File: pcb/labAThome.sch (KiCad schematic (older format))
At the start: 57 parts, among them J1 BME280, J10 SRV2, J11 GND, J2 SRV1, J3 5V, J4 24V IN, J5 SW&LED, J6 R1_CONN, J7 R2_CONN, J8 R3_CONN, J9 FAN, K1 G5V-2, K2 G5V-2, K3 G5V-2, Q1 IRLZ44N, Q2 IRLZ44N, Q3 IRLZ44N, SW1 RED, SW2 GREEN, SW3 BLACK, SW4 BLUE, SW5 WHITE, U1 HC-SR501, U2 24V->5V, U3 24V->3V3, U4 ESP32_DEVKITC_COMPATIBLE, U5 NE555

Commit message: Improved Layout
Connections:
- net labels added: 24V_PERM, Q1_D, Q2_D, R8_D4
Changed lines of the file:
@@
 	11150 6500 7500 6500
-Wire Notes Line
-	7300 6500 7300 2150
 Wire Notes Line
 	7500 2150 11150 2150
@@
 Wire Wire Line
 	7700 3700 7850 3700
+Text Label 7950 750  0    50   ~ 0
+24V_PERM
+Text Label 7550 1050 0    50   ~ 0
+Q2_D
+Text Label 6300 950  0    50   ~ 0
+Q1_D
+Text Label 6800 750  0    50   ~ 0
+R8_D4
+Wire Notes Line
+	7300 6500 7300 2150
 $EndSCHEMATC

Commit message: PCB REV2
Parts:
- removed C1: 100u, Capacitor_THT:CP_Radial_D5.0mm_P2.50mm, symbol Device:CP
- removed C2: 10n, Capacitor_THT:C_Disc_D5.0mm_W2.5mm_P2.50mm, symbol Device:C
- removed C3: u1, Capacitor_THT:C_Disc_D5.0mm_W2.5mm_P5.00mm, symbol Device:C
- removed J11: GND, Connector_PinHeader_2.54mm:PinHeader_1x08_P2.54mm_Vertical, symbol Connector_Generic:Conn_01x08
- removed R2: GL5528, OptoDevice:R_LDR_5.0x4.1mm_P3mm_Vertical, symbol Device:R_PHOTO
- removed U5: NE555, Package_DIP:DIP-8_W7.62mm, symbol Timer:NE555
- added J12: IO, Connector_PinHeader_2.54mm:PinHeader_2x04_P2.54mm_Vertical, symbol Connector_Generic:Conn_02x04_Odd_Even
- added Q4: BC547, Package_TO_SOT_THT:TO-92_Inline, symbol Transistor_BJT:BC547
- added R2: 3k3, Resistor_THT:R_Axial_DIN0207_L6.3mm_D2.5mm_P10.16mm_Horizontal, symbol Device:R
- added U6: GY-302, smopla:GY-302, symbol smopla:GY-302
- R1: value 10K -> 2k2
- R12: value 10k -> 1K
- RV1: value 100k -> R_POT
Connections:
- net labels added: IO0, IO1, IO2, IO3, IO4, IO5, POTI_T, R3_ON
- net labels removed: BRIGHTNESS
- wire segments 68 -> 42
- no-connect marks 23 -> 14
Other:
- note added: "check https://randomnerdtutorials.com/esp32-pinout-reference-gpios/"
- moved on the sheet: J1

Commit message: PCB V2 RC1
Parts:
- removed D5: 1N4001, Diode_THT:D_DO-41_SOD81_P10.16mm_Horizontal, symbol Diode:1N4001
- removed J12: IO, Connector_PinHeader_2.54mm:PinHeader_2x04_P2.54mm_Vertical, symbol Connector_Generic:Conn_02x04_Odd_Even
- removed J4: 24V IN, Connector_BarrelJack:BarrelJack_Horizontal, symbol Connector:Barrel_Jack_Switch
- removed Q1: IRLZ44N, Package_TO_SOT_THT:TO-220-3_Horizontal_TabDown, symbol Device:Q_NMOS_GDS
- removed R7: 10K, Resistor_THT:R_Axial_DIN0207_L6.3mm_D2.5mm_P10.16mm_Horizontal, symbol Device:R
- removed R8: 5R 1W, Resistor_THT:R_Axial_DIN0414_L11.9mm_D4.5mm_P15.24mm_Horizontal, symbol Device:R
- removed U3: 24V->3V3, sensact:MODULE_STEPDOWN, symbol sensact:MODULE_STEPDOWN
- added BZ1: Buzzer, Buzzer_Beeper:Buzzer_12x9.5RM7.6, symbol Device:Buzzer
- added J11: -, smopla:Banana_Jack_2mm, symbol Connector:Conn_01x01_Female
- added J12: FA2, Connector_PinHeader_2.54mm:PinHeader_1x03_P2.54mm_Vertical, symbol Connector_Generic:Conn_01x03
- added J13: Barrel_Jack_Switch, Connector_BarrelJack:BarrelJack_Horizontal, symbol Connector:Barrel_Jack_Switch
- added J14: FA3, Connector_PinHeader_2.54mm:PinHeader_1x03_P2.54mm_Vertical, symbol Connector_Generic:Conn_01x03
- added J4: +, smopla:Banana_Jack_2mm, symbol Connector:Conn_01x01_Female
- added JP2: 5V_ESP, Connector_PinHeader_2.54mm:PinHeader_1x02_P2.54mm_Vertical, symbol Device:Jumper_NO_Small
- added JP3: 3V3_5V, Jumper:SolderJumper-3_P2.0mm_Open_TrianglePad1.0x1.5mm_NumberLabels, symbol Jumper:SolderJumper_3_Open
- added U3: PDC004_Module, smopla:PDC004_Module, symbol smopla:PDC004_Module
- added U5: LD06AJSA, smopla:LD06AJSA, symbol smopla:LD06AJSA
- added U7: IPS_240_240, smopla:IPS_240_240, symbol smopla:IPS_240_240
- added U8: INMP441_Module, smopla:INMP441_Module, symbol smopla:INMP441_Module
- J9: value FAN -> FA1
- JP1: value 5V_LOCAL -> 5V_EXT
- R6: value 1K -> K1
- RV1: value R_POT -> DELAY_TIME
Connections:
- net labels added: BUZZER, FAN_SWITCH, I2S_SCK, I2S_SD, I2S_WS, LCD_BL, LCD_CLK, LCD_DC, LCD_MOSI
- net labels removed: 24V_PERM, IO0, IO1, IO2, IO3, IO4, IO5, Q1_D, R8_D4
- wire segments 42 -> 45
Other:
- note added: "Frei"
- note added: "Input Only"
- note added: "Input Only No Pull"
- note added: "Muss CLK"
- note added: "PULLED UP"
- note added: "Soll LED"
- note added: "Soll SW"
- note added: "WPD Soll Mosfet"
- moved on the sheet: D4, D8, J1, J10, J2, J3, J6, J7, J9, Q2, Q3, Q4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

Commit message: PCB V2 RC2
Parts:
- removed J11: -, smopla:Banana_Jack_2mm, symbol Connector:Conn_01x01_Female
- removed J4: +, smopla:Banana_Jack_2mm, symbol Connector:Conn_01x01_Female
- R1, R10, R12, R13, R14, R15, R16, R2, R3, R4, R5, R6, R9: footprint Resistor_THT:R_Axial_DIN0207_L6.3mm_D2.5mm_P10.16mm_Horizontal -> Resistor_THT:R_Axial_DIN0207_L6.3mm_D2.5mm_P7.62mm_Horizontal
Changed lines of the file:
@@
 F 0 "R3" V 1293 2100 50  0000 C CNN
 F 1 "68R" V 1384 2100 50  0000 C CNN
-F 2 "Resistor_THT:R_Axial_DIN0207_L6.3mm_D2.5mm_P10.16mm_Horizontal" V 1430 2100 50  0001 C CNN
+F 2 "Resistor_THT:R_Axial_DIN0207_L6.3mm_D2.5mm_P7.62mm_Horizontal" V 1430 2100 50  0001 C CNN
 F 3 "~" H 1500 2100 50  0001 C CNN
 	1    1500 2100
@@
 F 0 "R4" V 1293 2450 50  0000 C CNN
 F 1 "68R" V 1384 2450 50  0000 C CNN
-F 2 "Resistor_THT:R_Axial_DIN0207_L6.3mm_D2.5mm_P10.16mm_Horizontal" V 1430 2450 50  0001 C CNN
+F 2 "Resistor_THT:R_Axial_DIN0207_L6.3mm_D2.5mm_P7.62mm_Horizontal" V 1430 2450 50  0001 C CNN
 F 3 "~" H 1500 2450 50  0001 C CNN
 	1    1500 2450
@@
 F 0 "R5" V 1293 2850 50  0000 C CNN
 F 1 "68R" V 1384 2850 50  0000 C CNN
-F 2 "Resistor_THT:R_Axial_DIN0207_L6.3mm_D2.5mm_P10.16mm_Horizontal" V 1430 2850 50  0001 C CNN
+F 2 "Resistor_THT:R_Axial_DIN0207_L6.3mm_D2.5mm_P7.62mm_Horizontal" V 1430 2850 50  0001 C CNN
 F 3 "~" H 1500 2850 50  0001 C CNN
 	1    1500 2850
@@
 F 0 "R14" V 9143 6350 50  0000 C CNN
 F 1 "K1" V 9234 6350 50  0000 C CNN
-F 2 "Resistor_THT:R_Axial_DIN0207_L6.3mm_D2.5mm_P10.16mm_Horizontal" V 9280 6350 50  0001 C CNN
+F 2 "Resistor_THT:R_Axial_DIN0207_L6.3mm_D2.5mm_P7.62mm_Horizontal" V 9280 6350 50  0001 C CNN
 F 3 "~" H 9350 6350 50  0001 C CNN
 	1    9350 6350
@@
 F 0 "R13" V 9143 5950 50  0000 C CNN
 F 1 "K1" V 9234 5950 50  0000 C CNN
-F 2 "Resistor_THT:R_Axial_DIN0207_L6.3mm_D2.5mm_P10.16mm_Horizontal" V 9280 5950 50  0001 C CNN
+F 2 "Resistor_THT:R_Axial_DIN0207_L6.3mm_D2.5mm_P7.62mm_Horizontal" V 9280 5950 50  0001 C CNN
 F 3 "~" H 9350 5950 50  0001 C CNN
 	1    9350 5950
@@
 F 0 "R10" V 7200 1400 50  0000 C CNN
 F 1 "10K" V 7300 1400 50  0000 C CNN
-F 2 "Resistor_THT:R_Axial_DIN0207_L6.3mm_D2.5mm_P10.16mm_Horizontal" V 7230 1400 50  0001 C CNN
+F 2 "Resistor_THT:R_Axial_DIN0207_L6.3mm_D2.5mm_P7.62mm_Horizontal" V 7230 1400 50  0001 C CNN
 F 3 "~" H 7300 1400 50  0001 C CNN
 	1    7300 1400
@@
 F 0 "R9" V 7000 1250 50  0000 C CNN
 F 1 "1K" V 7100 1250 50  0000 C CNN
-F 2 "Resistor_THT:R_Axial_DIN0207_L6.3mm_D2.5mm_P10.16mm_Horizontal" V 7030 1250 50  0001 C CNN
+F 2 "Resistor_THT:R_Axial_DIN0207_L6.3mm_D2.5mm_P7.62mm_Horizontal" V 7030 1250 50  0001 C CNN
 F 3 "~" H 7100 1250 50  0001 C CNN
 	1    7100 1250
@@
 F 0 "R16" V 8550 1400 50  0000 C CNN
 F 1 "10K" V 8650 1400 50  0000 C CNN
-F 2 "Resistor_THT:R_Axial_DIN0207_L6.3mm_D2.5mm_P10.16mm_Horizontal" V 8580 1400 50  0001 C CNN
+F 2 "Resistor_THT:R_Axial_DIN0207_L6.3mm_D2.5mm_P7.62mm_Horizontal" V 8580 1400 50  0001 C CNN
 F 3 "~" H 8650 1400 50  0001 C CNN
 	1    8650 1400
@@
 F 0 "R15" V 8350 1250 50  0000 C CNN
 F 1 "1K" V 8450 1250 50  0000 C CNN
-F 2 "Resistor_THT:R_Axial_DIN0207_L6.3mm_D2.5mm_P10.16mm_Horizontal" V 8380 1250 50  0001 C CNN
+F 2 "Resistor_THT:R_Axial_DIN0207_L6.3mm_D2.5mm_P7.62mm_Horizontal" V 8380 1250 50  0001 C CNN
 F 3 "~" H 8450 1250 50  0001 C CNN
 	1    8450 1250
@@
 F 0 "R12" V 8400 4050 50  0000 C CNN
 F 1 "1K" V 8500 4050 50  0000 C CNN
-F 2 "Resistor_THT:R_Axial_DIN0207_L6.3mm_D2.5mm_P10.16mm_Horizontal" V 8430 4050 50  0001 C CNN
+F 2 "Resistor_THT:R_Axial_DIN0207_L6.3mm_D2.5mm_P7.62mm_Horizontal" V 8430 4050 50  0001 C CNN
 F 3 "~" H 8500 4050 50  0001 C CNN
 	1    8500 4050
@@
 F 0 "R1" V 10200 5050 50  0000 C CNN
 F 1 "2k2" V 10300 5050 50  0000 C CNN
-F 2 "Resistor_THT:R_Axial_DIN0207_L6.3mm_D2.5mm_P10.16mm_Horizontal" V 10230 5050 50  0001 C CNN
+F 2 "Resistor_THT:R_Axial_DIN0207_L6.3mm_D2.5mm_P7.62mm_Horizontal" V 10230 5050 50  0001 C CNN
 F 3 "~" H 10300 5050 50  0001 C CNN
 	1    10300 5050
@@
 F 0 "R2" V 10200 5350 50  0000 C CNN
 F 1 "3k3" V 10300 5350 50  0000 C CNN
-F 2 "Resistor_THT:R_Axial_DIN0207_L6.3mm_D2.5mm_P10.16mm_Horizontal" V 10230 5350 50  0001 C CNN
+F 2 "Resistor_THT:R_Axial_DIN0207_L6.3mm_D2.5mm_P7.62mm_Horizontal" V 10230 5350 50  0001 C CNN
 F 3 "~" H 10300 5350 50  0001 C CNN
 	1    10300 5350
@@
 F 0 "R6" V 1100 5400 50  0000 C CNN
 F 1 "K1" V 1200 5400 50  0000 C CNN
-F 2 "Resistor_THT:R_Axial_DIN0207_L6.3mm_D2.5mm_P10.16mm_Horizontal" V 1130 5400 50  0001 C CNN
+F 2 "Resistor_THT:R_Axial_DIN0207_L6.3mm_D2.5mm_P7.62mm_Horizontal" V 1130 5400 50  0001 C CNN
 F 3 "~" H 1200 5400 50  0001 C CNN
 	1    1200 5400
@@
 Wire Wire Line
 	1400 3250 1800 3250
-$Comp
-L Connector:Conn_01x01_Female J4
-U 1 1 5EE6991E
-P 3500 1500
-F 0 "J4" H 3528 1526 50  0000 L CNN
-F 1 "+" H 3700 1500 50  0000 L CNN
-F 2 "smopla:Banana_Jack_2mm" H 3500 1500 50  0001 C CNN
-F 3 "~" H 3500 1500 50  0001 C CNN
-	1    3500 1500
-	1    0    0    -1
-$EndComp
-$Comp
-L Connector:Conn_01x01_Female J11
-U 1 1 5EE6A720
-P 3500 1600
-F 0 "J11" H 3528 1626 50  0000 L CNN
-F 1 "-" H 3700 1600 50  0000 L CNN
-F 2 "smopla:Banana_Jack_2mm" H 3500 1600 50  0001 C CNN
-F 3 "~" H 3500 1600 50  0001 C CNN
-	1    3500 1600
-	1    0    0    -1
-$EndComp
 Wire Wire Line
 	3050 1500 3300 1500
-Connection ~ 3300 1500
 Wire Wire Line
 	3300 1600 3050 1600
-Connection ~ 3300 1600
 $Comp
 L Connector_Generic:Conn_01x03 J12

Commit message: PCB V2 as ordered
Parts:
- added J4: EXTENSION, Connector_JST:JST_XH_B4B-XH-A_1x04_P2.50mm_Vertical, symbol Connector:Conn_01x04_Male
- added SW6: FAN, smopla:MTS-102, symbol Switch:SW_SPDT
- U7: value IPS_240_240 -> Display
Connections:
- net +5V: now also J4.1 (Pin_1)
- net GND: now also J4.4 (Pin_4), SW6.2 (B); no longer J12.1 (Pin_1)
- net R3_12: now also J14.2 (Pin_2)
- net R3_22: no longer J14.2 (Pin_2)
- net SCL: now also J4.3 (Pin_3)
- net SDA: now also J4.2 (Pin_2)
- new net: J12.1 (Pin_1), SW6.3 (C)
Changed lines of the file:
@@
 P 1300 7150
 F 0 "U7" H 1528 7001 50  0000 L CNN
-F 1 "IPS_240_240" H 1528 6910 50  0000 L CNN
+F 1 "Display" H 1528 6910 50  0000 L CNN
 F 2 "smopla:IPS_240_240" H 1300 7150 50  0001 C CNN
 F 3 "" H 1300 7150 50  0001 C CNN
@@
 L power:GND #PWR048
 U 1 1 5EEDC087
-P 10400 1400
-F 0 "#PWR048" H 10400 1150 50  0001 C CNN
-F 1 "GND" V 10405 1272 50  0000 R CNN
-F 2 "" H 10400 1400 50  0001 C CNN
-F 3 "" H 10400 1400 50  0001 C CNN
-	1    10400 1400
+P 10000 1300
+F 0 "#PWR048" H 10000 1050 50  0001 C CNN
+F 1 "GND" V 10005 1172 50  0000 R CNN
+F 2 "" H 10000 1300 50  0001 C CNN
+F 3 "" H 10000 1300 50  0001 C CNN
+	1    10000 1300
 	0    1    1    0
 $EndComp
@@
 NoConn ~ 8150 3750
 Text GLabel 8150 3650 0    50   BiDi ~ 0
-R3_22
+R3_12
+$Comp
+L Switch:SW_SPDT SW6
+U 1 1 5EED61B0
+P 10200 1300
+F 0 "SW6" H 10200 1585 50  0000 C CNN
+F 1 "FAN" H 10200 1494 50  0000 C CNN
+F 2 "smopla:MTS-102" H 10200 1300 50  0001 C CNN
+F 3 "~" H 10200 1300 50  0001 C CNN
+	1    10200 1300
+	1    0    0    -1
+$EndComp
+$Comp
+L Connector:Conn_01x04_Male J4
+U 1 1 5EF6E56D
+P 1800 4800
+F 0 "J4" H 1772 4774 50  0000 R CNN
+F 1 "EXTENSION" H 1772 4683 50  0000 R CNN
+F 2 "Connector_JST:JST_XH_B4B-XH-A_1x04_P2.50mm_Vertical" H 1800 4800 50  0001 C CNN
+F 3 "~" H 1800 4800 50  0001 C CNN
+	1    1800 4800
+	-1   0    0    -1
+$EndComp
+Text GLabel 1600 4800 0    50   BiDi ~ 0
+SDA
+$Comp
+L power:GND #PWR050
+U 1 1 5EF73FB6
+P 1600 5000
+F 0 "#PWR050" H 1600 4750 50  0001 C CNN
+F 1 "GND" V 1605 4872 50  0000 R CNN
+F 2 "" H 1600 5000 50  0001 C CNN
+F 3 "" H 1600 5000 50  0001 C CNN
+	1    1600 5000
+	0    1    1    0
+$EndComp
+Text GLabel 1600 4900 0    50   BiDi ~ 0
+SCL
+$Comp
+L power:+5V #PWR0114
+U 1 1 5EFABFF1
+P 1600 4700
+F 0 "#PWR0114" H 1600 4550 50  0001 C CNN
+F 1 "+5V" V 1615 4828 50  0000 L CNN
+F 2 "" H 1600 4700 50  0001 C CNN
+F 3 "" H 1600 4700 50  0001 C CNN
+	1    1600 4700
+	0    -1   -1   0
+$EndComp
 $EndSCHEMATC

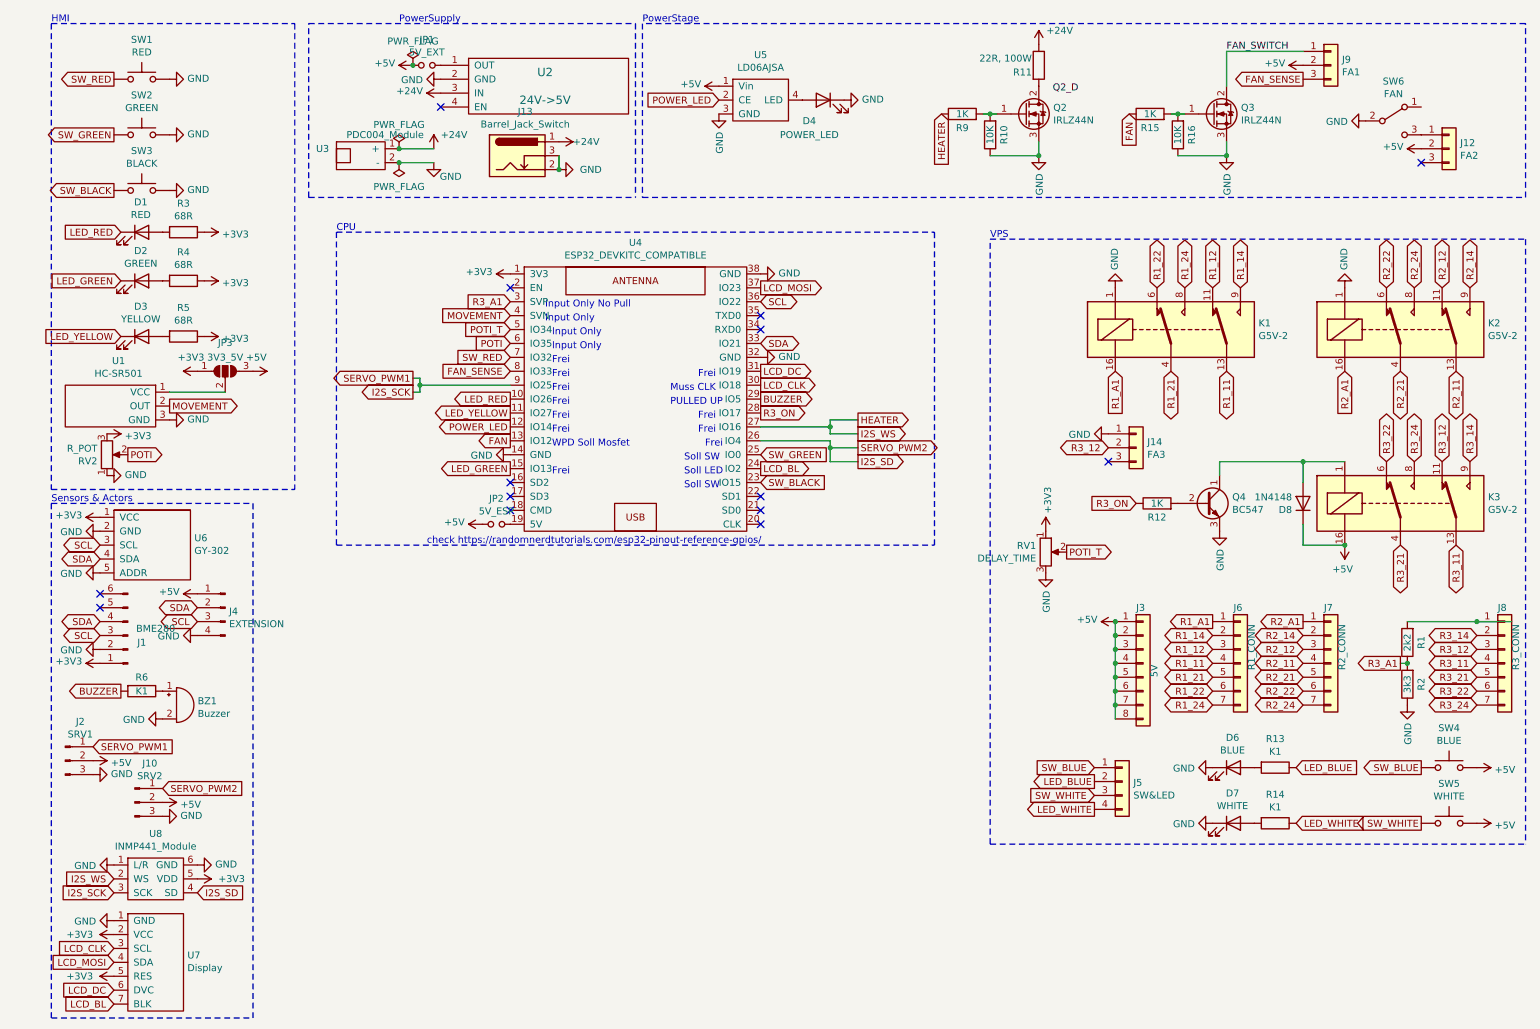
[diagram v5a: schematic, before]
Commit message: DoubleRow VPS connector; Various 3D models
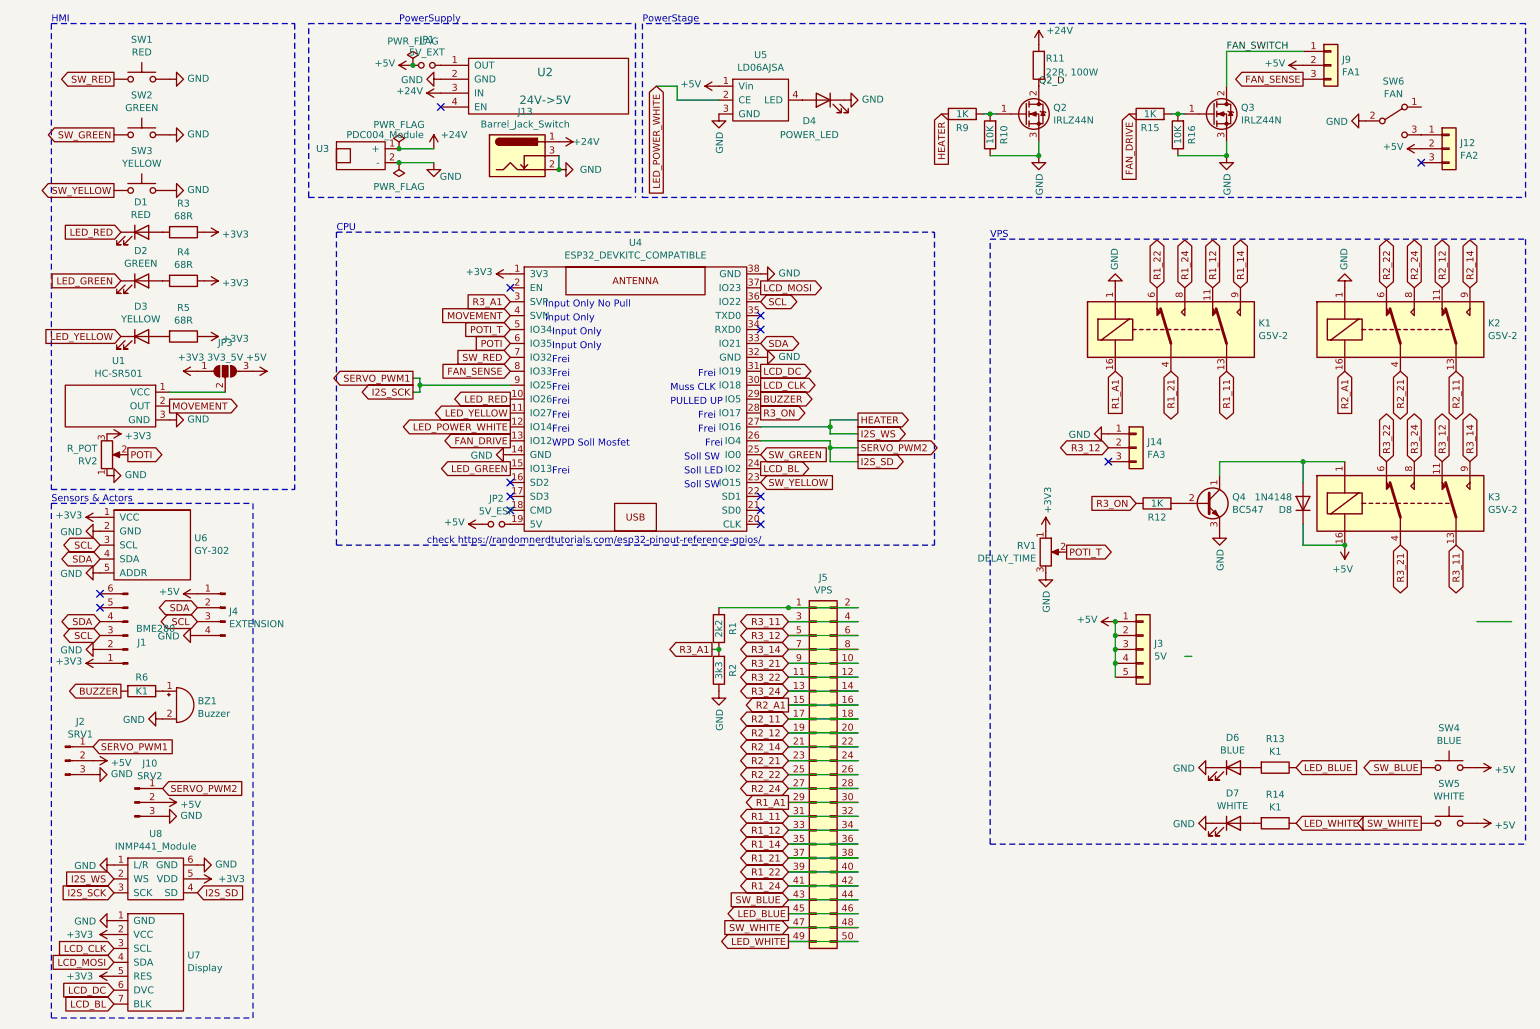
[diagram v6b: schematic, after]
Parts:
- removed J3: 5V, Connector_PinHeader_2.54mm:PinHeader_1x08_P2.54mm_Vertical, symbol Connector_Generic:Conn_01x08
- removed J5: SW&LED, Connector_PinHeader_2.54mm:PinHeader_1x04_P2.54mm_Vertical, symbol Connector_Generic:Conn_01x04
- removed J6: R1_CONN, Connector_PinHeader_2.54mm:PinHeader_1x07_P2.54mm_Vertical, symbol Connector_Generic:Conn_01x07
- removed J7: R2_CONN, Connector_PinHeader_2.54mm:PinHeader_1x07_P2.54mm_Vertical, symbol Connector_Generic:Conn_01x07
- removed J8: R3_CONN, Connector_PinHeader_2.54mm:PinHeader_1x07_P2.54mm_Vertical, symbol Connector_Generic:Conn_01x07
- added J3: 5V, Connector_PinHeader_2.54mm:PinHeader_1x05_P2.54mm_Vertical, symbol Connector_Generic:Conn_01x05
- added J5: VPS, Connector_PinHeader_2.54mm:PinHeader_2x25_P2.54mm_Vertical, symbol Connector_Generic:Conn_02x25_Odd_Even
- J12, J14, J9: footprint Connector_PinHeader_2.54mm:PinHeader_1x03_P2.54mm_Vertical -> Connector:FanPinHeader_1x03_P2.54mm_Vertical
- SW3: value BLACK -> YELLOW
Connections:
- net labels added: FAN_DRIVE, LED_POWER_WHITE, SW_YELLOW
- net labels removed: FAN, POWER_LED, SW_BLACK
- wire segments 45 -> 71
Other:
- moved on the sheet: R1, R2
